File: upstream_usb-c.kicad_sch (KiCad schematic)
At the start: 1 part

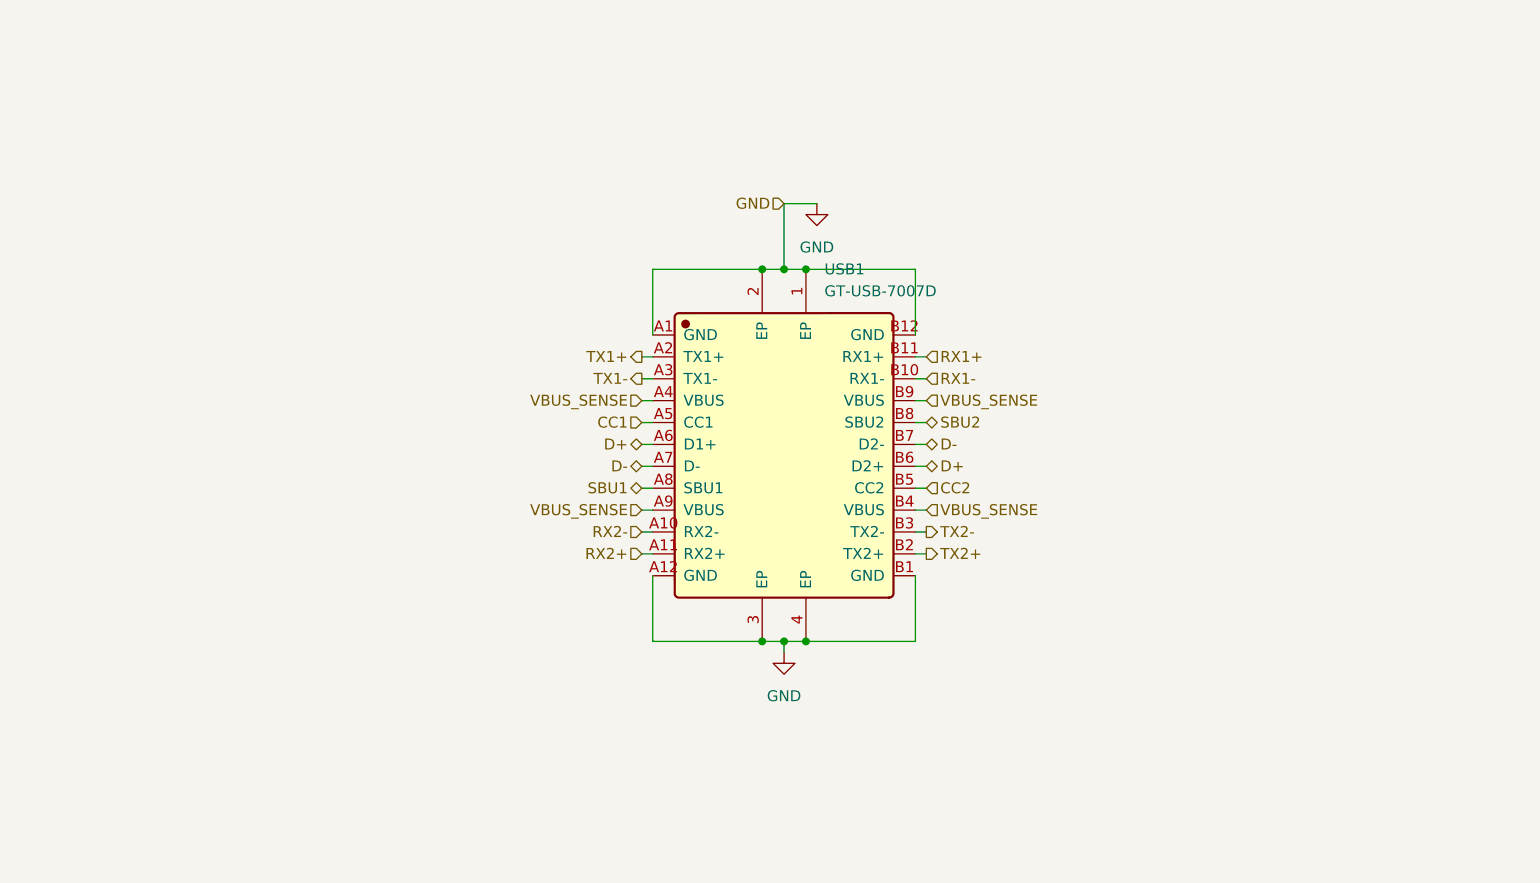
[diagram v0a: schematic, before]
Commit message: Added TVS clamping diodes to upstream USB-C port and fixed RX/TX orientation routing for entire system
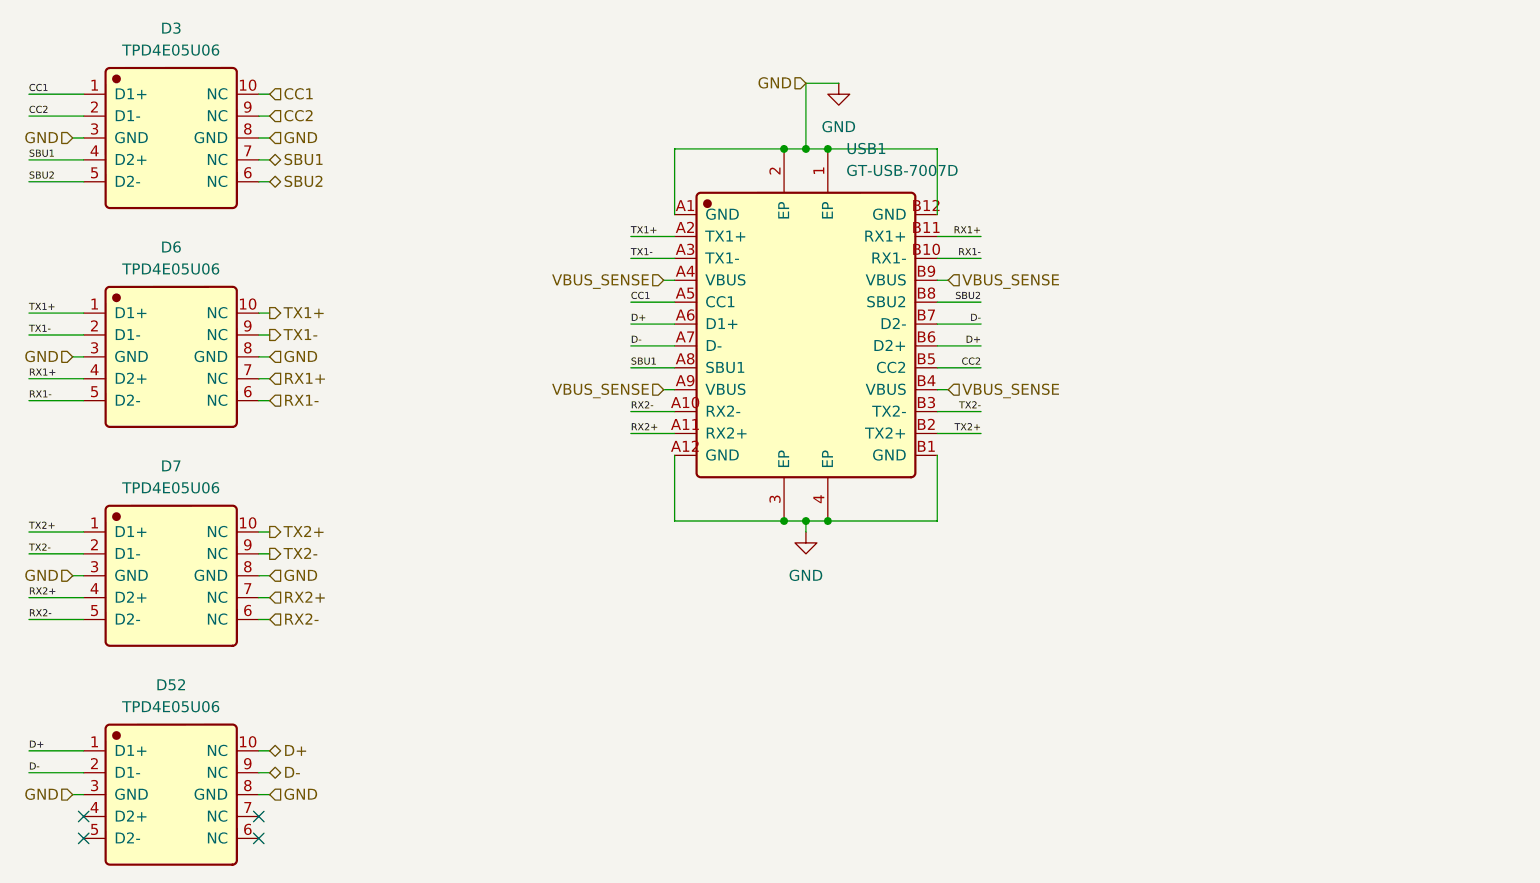
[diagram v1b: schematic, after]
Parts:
- added D3, D52, D6, D7: TPD4E05U06, JLCImport:TPD4E05U06DQAR_C138714, symbol JLCImport:TPD4E05U06DQAR_C138714
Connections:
- net CC1: now also D3.1 (D1+), D3.10 (NC)
- net CC2: now also D3.2 (D1-), D3.9 (NC)
- net D+: now also D52.1 (D1+), D52.10 (NC)
- net D-: now also D52.2 (D1-), D52.9 (NC)
- net GND: now also D3.3 (GND), D3.8 (GND), D52.3 (GND), D52.8 (GND), D6.3 (GND), D6.8 (GND), D7.3 (GND), D7.8 (GND)
- net RX1+: now also D6.4 (D2+), D6.7 (NC)
- net RX1-: now also D6.5 (D2-), D6.6 (NC)
- net RX2+: now also D7.4 (D2+), D7.7 (NC)
- net RX2-: now also D7.5 (D2-), D7.6 (NC)
- net SBU1: now also D3.4 (D2+), D3.7 (NC)
- net SBU2: now also D3.5 (D2-), D3.6 (NC)
- net TX1+: now also D6.1 (D1+), D6.10 (NC)
- net TX1-: now also D6.2 (D1-), D6.9 (NC)
- net TX2+: now also D7.1 (D1+), D7.10 (NC)
- net TX2-: now also D7.2 (D1-), D7.9 (NC)
- no-connect marks 0 -> 4
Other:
- moved on the sheet: USB1

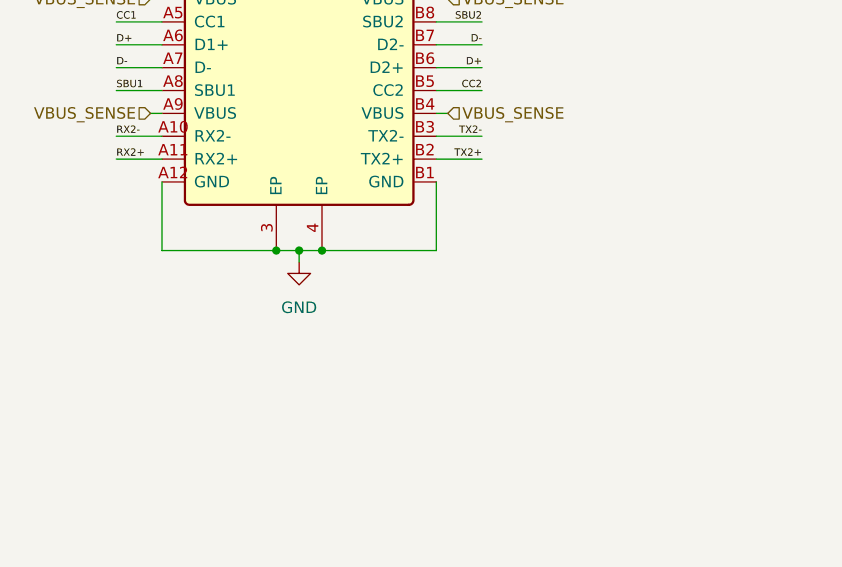
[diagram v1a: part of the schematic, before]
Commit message: Added an (optional) RC network between shield pins of USB connector and GND
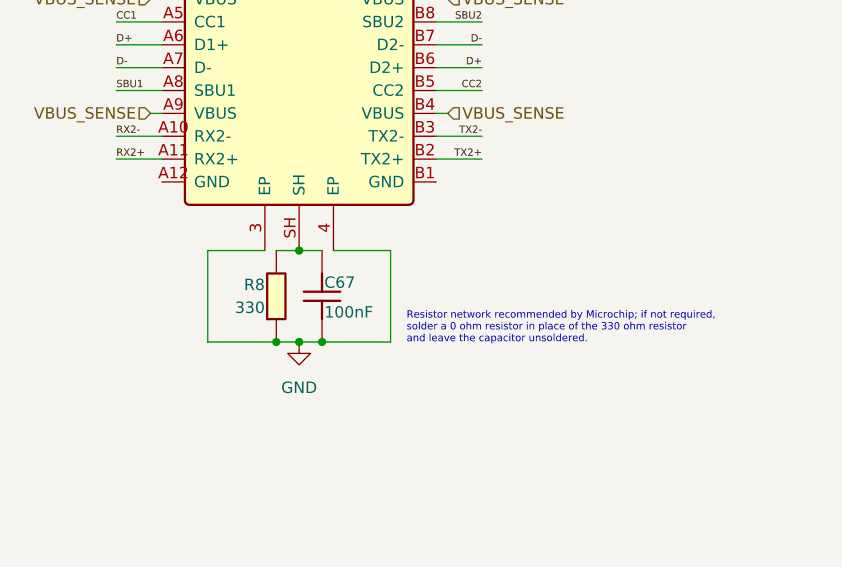
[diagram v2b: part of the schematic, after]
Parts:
- added C67: 100nF, Capacitor_SMD:C_0402_1005Metric, symbol JLCImport:CL05B104KB54PNC
- added R8: 330, Resistor_SMD:R_0402_1005Metric, symbol JLCImport:0402WGF3300TCE
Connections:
- net GND: now also C67.1, R8.1; no longer USB1.A12 (GND), USB1.B1 (GND)
- new net: C67.2, R8.2, USB1.SH
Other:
- note added: "Resistor network recommended by Microchip; if not required, solder a 0 ohm resistor in place of the 330 ohm resistor and leave the capacitor unsoldered."

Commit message: Basic Function Review/Documentation of RP2354B
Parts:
- added C207: 1uF, Capacitor_SMD:C_0603_1608Metric, symbol JLCImport:CL10A105KB8NNNC
- added C209: 4.7uF, Capacitor_SMD:C_0603_1608Metric, symbol JLCImport:CL10A475KL8NRNC
- added C84, C85, C87, C88: 10nF, Capacitor_SMD:C_0402_1005Metric, symbol JLCImport:TCC0402X7R103M500AT
- added D53: PMEG3020EH, Diode_SMD:D_SOD-123F, symbol Diode:PMEG3020EH
- added LED13: White, JLCImport:GL0603UW01, symbol JLCImport:GL0603UW01
- added R194: 3.48, Resistor_SMD:R_0603_1608Metric, symbol JLCImport:RS-03L3R48FT
- added R222: 10k, Resistor_SMD:R_0402_1005Metric, symbol JLCImport:0402WGF1002TCE
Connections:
- net GND: now also C207.1, C84.1, C85.1, C87.1, C88.1, D53.2 (A), LED13.2 (C), R194.1
- net VBUS_SENSE renamed VBUS
- net VBUS: now also C207.2, C209.1, C84.2, C85.2, C87.2, C88.2, D53.1 (K), R222.2
- new net: LED13.1 (A), R222.1
- new net: C209.2, R194.2
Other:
- moved on the sheet: C67, R8, USB1

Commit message: Basic Function Review/Documentation for TPS65987D
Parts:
- removed D53: PMEG3020EH, Diode_SMD:D_SOD-123F, symbol Diode:PMEG3020EH
- added U15: ESTVS2200DRVR, JLCImport:ESTVS2200DRVR, symbol JLCImport:ESTVS2200DRVR
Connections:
- net GND: now also U15.1 (GND), U15.2 (GND), U15.3 (GND), U15.7 (EP)
- net VBUS: now also U15.4 (VDD/IO), U15.5 (VDD/IO), U15.6 (VDD/IO)
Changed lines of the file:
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@@
 	)
 	(junction
-		(at 170.18 44.45)
+		(at 132.08 44.45)
 		(diameter 0)
 		(color 0 0 0 0)
 	)
 	(junction
-		(at 170.18 24.13)
+		(at 170.18 44.45)
 		(diameter 0)
 		(color 0 0 0 0)
 	)
 	(junction
-		(at 127 24.13)
+		(at 170.18 24.13)
 		(diameter 0)
 		(color 0 0 0 0)
@@
 	)
 	(junction
-		(at 132.08 44.45)
+		(at 82.55 25.4)
 		(diameter 0)
 		(color 0 0 0 0)
 	)
 	(junction
-		(at 82.55 25.4)
+		(at 85.09 78.74)
 		(diameter 0)
 		(color 0 0 0 0)
 	)
 	(junction
-		(at 85.09 78.74)
+		(at 139.7 59.69)
 		(diameter 0)
 		(color 0 0 0 0)
@@
 	)
 	(junction
+		(at 132.08 24.13)
+		(diameter 0)
+		(color 0 0 0 0)
+	)
+	(junction
 		(at 80.01 25.4)
 		(diameter 0)
@@
 	)
 	(junction
-		(at 144.78 44.45)
+		(at 165.1 62.23)
 		(diameter 0)
 		(color 0 0 0 0)
 	)
 	(junction
-		(at 144.78 24.13)
+		(at 144.78 44.45)
 		(diameter 0)
 		(color 0 0 0 0)
 	)
 	(junction
-		(at 132.08 24.13)
+		(at 144.78 24.13)
 		(diameter 0)
 		(color 0 0 0 0)
 	)
 	(junction
-		(at 151.13 44.45)
+		(at 139.7 62.23)
 		(diameter 0)
 		(color 0 0 0 0)
 	)
 	(junction
-		(at 127 44.45)
+		(at 151.13 44.45)
 		(diameter 0)
 		(color 0 0 0 0)
@@
 	(wire
 		(pts
-			(xy 127 24.13) (xy 132.08 24.13)
-		)
-		(stroke
-			(width 0)
-			(type default)
-		)
-	)
-	(wire
-		(pts
 			(xy 158.75 24.13) (xy 170.18 24.13)
 		)
@@
 	(wire
 		(pts
-			(xy 127 38.1) (xy 127 44.45)
-		)
-		(stroke
-			(width 0)
-			(type default)
-		)
-	)
-	(wire
-		(pts
 			(xy 97.79 25.4) (xy 97.79 33.02)
 		)
@@
 	(wire
 		(pts
-			(xy 66.04 53.34) (xy 67.31 53.34)
+			(xy 139.7 59.69) (xy 139.7 62.23)
 		)
 		(stroke
@@
 	(wire
 		(pts
-			(xy 127 24.13) (xy 127 30.48)
+			(xy 66.04 53.34) (xy 67.31 53.34)
 		)
 		(stroke
@@
 	(wire
 		(pts
-			(xy 127 44.45) (xy 132.08 44.45)
+			(xy 139.7 62.23) (xy 139.7 64.77)
+		)
+		(stroke
+			(width 0)
+			(type default)
+		)
+	)
+	(wire
+		(pts
+			(xy 151.13 54.61) (xy 139.7 54.61)
 		)
 		(stroke
@@
 	(wire
 		(pts
-			(xy 125.73 44.45) (xy 127 44.45)
+			(xy 130.81 44.45) (xy 132.08 44.45)
 		)
 		(stroke
@@
 	(wire
 		(pts
-			(xy 125.73 24.13) (xy 127 24.13)
+			(xy 130.81 24.13) (xy 132.08 24.13)
 		)
 		(stroke
@@
 	(wire
 		(pts
+			(xy 165.1 59.69) (xy 165.1 62.23)
+		)
+		(stroke
+			(width 0)
+			(type default)
+		)
+	)
+	(wire
+		(pts
 			(xy 138.43 24.13) (xy 144.78 24.13)
 		)
@@
 	(wire
 		(pts
+			(xy 139.7 54.61) (xy 139.7 59.69)
+		)
+		(stroke
+			(width 0)
+			(type default)
+		)
+	)
+	(wire
+		(pts
 			(xy 82.55 17.78) (xy 86.36 17.78)
 		)
@@
 	(wire
 		(pts
+			(xy 165.1 62.23) (xy 165.1 64.77)
+		)
+		(stroke
+			(width 0)
+			(type default)
+		)
+	)
+	(wire
+		(pts
 			(xy 25.4 54.61) (xy 26.67 54.61)
 		)
@@
 	(hierarchical_label "GND"
 		(shape input)
-		(at 125.73 44.45 180)
+		(at 130.81 44.45 180)
 		(effects
 			(font
@@
 	(hierarchical_label "VBUS"
 		(shape input)
+		(at 165.1 62.23 0)
+		(effects
+			(font
+				(size 1.27 1.27)
+			)
+			(justify left)
+		)
+	)
+	(hierarchical_label "VBUS"
+		(shape input)
 		(at 66.04 40.64 180)
 		(effects
@@
 	(hierarchical_label "VBUS"
 		(shape input)
-		(at 125.73 24.13 180)
+		(at 130.81 24.13 180)
 		(effects
 			(font
@@
 		)
 	)
+	(hierarchical_label "GND"
+		(shape input)
+		(at 139.7 62.23 180)
+		(effects
+			(font
+				(size 1.27 1.27)
+			)
+			(justify right)
+		)
+	)
 	(hierarchical_label "RX2+"
 		(shape input)
@@
 	)
 	(symbol
+		(lib_id "JLCImport:ESTVS2200DRVR")
+		(at 151.13 62.23 0)
+		(unit 1)
+		(body_style 1)
+		(exclude_from_sim no)
+		(in_bom yes)
+		(on_board yes)
+		(in_pos_files yes)
+		(dnp no)
+		(fields_autoplaced yes)
+		(property "Reference" "U15"
+			(at 152.4 69.85 0)
+			(show_name no)
+			(do_not_autoplace no)
+			(effects
+				(font
+					(size 1.27 1.27)
+				)
+			)
+		)
+		(property "Value" "ESTVS2200DRVR"
+			(at 152.4 72.39 0)
+			(show_name no)
+			(do_not_autoplace no)
+			(effects
+				(font
+					(size 1.27 1.27)
+				)
+			)
+		)
+		(property "Footprint" "JLCImport:ESTVS2200DRVR"
+			(at 151.13 62.23 0)
+			(hide yes)
+			(show_name no)
+			(do_not_autoplace no)
+			(effects
+				(font
+					(size 1.27 1.27)
+				)
+			)
+		)
+		(property "Datasheet" "https://www.lcsc.com/datasheet/lcsc_datasheet_2504101957_ElecSuper-ESTVS2200DRVR_C42400188.pdf"
+			(at 151.13 62.23 0)
+			(hide yes)
+			(show_name no)
+			(do_not_autoplace no)
+			(effects
+				(font
+					(size 1.27 1.27)
+				)
+			)
+		)
+		(property "Description" "115pF 22V 25.8V 28.6V 2kW@8/20us 500pA 70A@8/20us IEC 61000-4-2、IEC 61000-4-5、IEC 61000-4-4 DFN-6-EP(2x2) ESD and Surge Protection (TVS/ESD) ROHS"
+			(at 151.13 62.23 0)
+			(hide yes)
+			(show_name no)
+			(do_not_autoplace no)
+			(effects
+				(font
+					(size 1.27 1.27)
+				)
+			)
+		)
+		(property "LCSC" "C42400188"
+			(at 151.13 62.23 0)
+			(hide yes)
+			(show_name no)
+			(do_not_autoplace no)
+			(effects
+				(font
+					(size 1.27 1.27)
+				)
+			)
+		)
+		(property "Manufacturer" "ElecSuper"
+			(at 151.13 62.23 0)
+			(hide yes)
+			(show_name no)
+			(do_not_autoplace no)
+			(effects
+				(font
+					(size 1.27 1.27)
+				)
+			)
+		)
+		(property "Manufacturer Part" "ESTVS2200DRVR"
+			(at 151.13 62.23 0)
+			(hide yes)
+			(show_name no)
+			(do_not_autoplace no)
+			(effects
+				(font
+					(size 1.27 1.27)
+				)
+			)
+		)
+		(pin "1"
+		)
+		(pin "5"
+		)
+		(pin "7"
+		)
+		(pin "3"
+		)
+		(pin "2"
+		)
+		(pin "4"
+		)
+		(pin "6"
+		)
+		(instances
+			(project "serverv2_backplane"
+				(path "/d38d6818-cf53-410d-afa3-a75a85b7c05a/3c4f89a0-50a7-4973-9d07-1756122c8dda"
+					(reference "U15")
+					(unit 1)
+				)
+			)
+		)
+	)
+	(symbol
 		(lib_id "JLCImport:0402WGF3300TCE")
 		(at 80.01 73.66 90)
@@
 					(unit 1)
 				)
-			)
-		)
-	)
-	(symbol
-		(lib_id "Diode:PMEG3020EH")
-		(at 127 34.29 270)
-		(unit 1)
-		(body_style 1)
-		(exclude_from_sim no)
-		(in_bom yes)
-		(on_board yes)
-		(in_pos_files yes)
-		(dnp no)
-		(property "Reference" "D53"
-			(at 124.968 34.29 90)
-			(show_name no)
-			(do_not_autoplace no)
-			(effects
-				(font
-					(size 1.27 1.27)
-				)
-				(justify right)
-			)
-		)
-		(property "Value" "PMEG3020EH"
-			(at 129.54 35.2424 90)
-			(hide yes)
-			(show_name no)
-			(do_not_autoplace no)
-			(effects
-				(font
-					(size 1.27 1.27)
-				)
-				(justify left)
-			)
-		)
-		(property "Footprint" "Diode_SMD:D_SOD-123F"
-			(at 122.555 34.29 0)
-			(hide yes)
-			(show_name no)
-			(do_not_autoplace no)
-			(effects
-				(font
-					(size 1.27 1.27)
-				)
-			)
-		)
-		(property "Datasheet" "https://assets.nexperia.com/documents/data-sheet/PMEG3020EH_EJ.pdf"
-			(at 127 34.29 0)
-			(hide yes)
-			(show_name no)
-			(do_not_autoplace no)
-			(effects
-				(font
-					(size 1.27 1.27)
-				)
-			)
-		)
-		(property "Description" "30V, 2A ultra low Vf MEGA Schottky barrier rectifier, SOD-123F"
-			(at 127 34.29 0)
-			(hide yes)
-			(show_name no)
-			(do_not_autoplace no)
-			(effects
-				(font
-					(size 1.27 1.27)
-				)
-			)
-		)
-		(property "LCSC" "C52747979"
-			(at 127 34.29 90)
-			(hide yes)
-			(show_name no)
-			(do_not_autoplace no)
-			(effects
-				(font
-					(size 1.27 1.27)
-				)
-			)
-		)
-		(property "MPN" "PMEG3020EH-FS"
-			(at 127 34.29 90)
-			(hide yes)
-			(show_name no)
-			(do_not_autoplace no)
-			(effects
-				(font
-					(size 1.27 1.27)
-				)
-			)
-		)
-		(property "Manufacturer" "FUXINSEMI"
-			(at 127 34.29 90)
-			(hide yes)
-			(show_name no)
-			(do_not_autoplace no)
-			(effects
-				(font
-					(size 1.27 1.27)
-				)
-			)
-		)
-		(pin "1"
-		)
-		(pin "2"
-		)
-		(instances
-			(project "serverv2_backplane"
-				(path "/d38d6818-cf53-410d-afa3-a75a85b7c05a/3c4f89a0-50a7-4973-9d07-1756122c8dda"
-					(reference "D53")
-					(unit 1)
-				)
